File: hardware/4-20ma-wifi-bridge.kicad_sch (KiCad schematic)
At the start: 16 parts, among them J1 Conn_01x19_Female, J2 Conn_01x19_Female, J3 Screw_Terminal_01x02, J4 Screw_Terminal_01x02, M1 DC-DC_Buck_Step_Module-dc-dc_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, SW1 SW_DIP_x01, U1 ESP32-DEVKITC-32D, U2 INA196

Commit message: Added kicad design files
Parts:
- removed U1: ESP32-DEVKITC-32D, MODULE_ESP32-DEVKITC-32D, symbol ESP32-DEVKITC-32D:ESP32-DEVKITC-32D
- removed U2: INA196, Package_TO_SOT_SMD:SOT-23-5, symbol Amplifier_Current:INA196
- added D2: LED, LED_THT:LED_D3.0mm_FlatTop, symbol Device:LED
- added D3, D4: 1N4004, Diode_SMD:D_SMA, symbol Diode:1N4004
- added D5: LED, LED_THT:LED_D1.8mm_W1.8mm_H2.4mm_Horizontal_O1.27mm_Z1.6mm, symbol Device:LED
- added J3, J4: Screw_Terminal_01x02, project_library:TerminalBlock__1x02_P5.00mm_90Degree, symbol Connector:Screw_Terminal_01x02
- added K1, K2: G5V-1, Relay_THT:Relay_SPDT_Omron_G5V-1, symbol Relay:G5V-1
- added Q1, Q2: 2N7002E, Package_TO_SOT_SMD:SOT-23, symbol Transistor_FET:2N7002E
- added R1, R2, R3, R5: 1k, Resistor_SMD:R_0805_2012Metric_Pad1.20x1.40mm_HandSolder, symbol Device:R
- added R4, R6: 10k, Resistor_SMD:R_0805_2012Metric_Pad1.20x1.40mm_HandSolder, symbol Device:R
- added TP1, TP2, TP3: TestPoint, TestPoint:TestPoint_Pad_D1.0mm, symbol Connector:TestPoint
- added U1: ESP32-DEVKITC-32U, MODULE_ESP32-DEVKITC-32U, symbol ESP32-DEVKITC-32U:ESP32-DEVKITC-32U
- added U2: LMP8640, Package_TO_SOT_SMD:SOT-23-6, symbol Amplifier_Current:LMP8640
- D1: footprint LED_THT:LED_D1.8mm_W1.8mm_H2.4mm_Horizontal_O1.27mm_Z4.9mm -> LED_THT:LED_D3.0mm_FlatTop
- R10: renamed from R4; value 4.99 -> 2.7ohm; footprint Resistor_SMD:R_0805_2012Metric_Pad1.20x1.40mm_HandSolder -> Resistor_SMD:R_2512_6332Metric_Pad1.40x3.35mm_HandSolder
- R7: renamed from R1; value 250 -> 1k
- R8: renamed from R2; value 250 -> 1k
- R9: renamed from R3; value 4.99 -> 10k
- renumbered D2 to D6, J3 to J5, J4 to J6
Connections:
- net +3V3: now also TP2.1
- net +5V: now also D3.1 (K), D4.1 (K), K1.2, K2.2, R3.2, R5.2, TP1.1, U2.6 (V+)
- net GND: now also Q1.2 (S), Q2.2 (S), R4.2, R6.2, U2.2 (V-)
- net led1: now also J2.17 (Pin_17), D5.1 (K); no longer D1.1 (K), J2.9 (Pin_9)
- net led2: now also J2.18 (Pin_18); no longer J2.10 (Pin_10)
- net switch: now also J2.19 (Pin_19); no longer J2.2 (Pin_2)
- net vsens: now also J1.3 (Pin_3), TP3.1, U2.1; no longer J1.5 (Pin_5)
- net at R7.1: now also D5.2 (A); no longer D1.2 (A)
- net relay1: now reaches J1.10 (Pin_10)
- net relay1: now also R2.2
- net relay2: now reaches J1.11 (Pin_11)
- net relay2: now also R1.2
- net at J6.1 (Pin_1), R10.1: now also U2.3 (+)
- net at J6.2 (Pin_2), R10.2: now also U2.4 (-)
- new net: J4.1 (Pin_1), K2.5, K2.6
- new net: J4.2 (Pin_2), K2.10
- new net: D2.1 (K), D4.2 (A), K2.9, Q2.3 (D)
- new net: D1.1 (K), D3.2 (A), K1.9, Q1.3 (D)
- new net: Q1.1 (G), R2.1, R4.1
- new net: Q2.1 (G), R1.1, R6.1
- new net: J3.2 (Pin_2), K1.10
- new net: J3.1 (Pin_1), K1.5, K1.6
- new net: D1.2 (A), R3.1
- new net: D2.2 (A), R5.1
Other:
- moved on the sheet: J1, J2

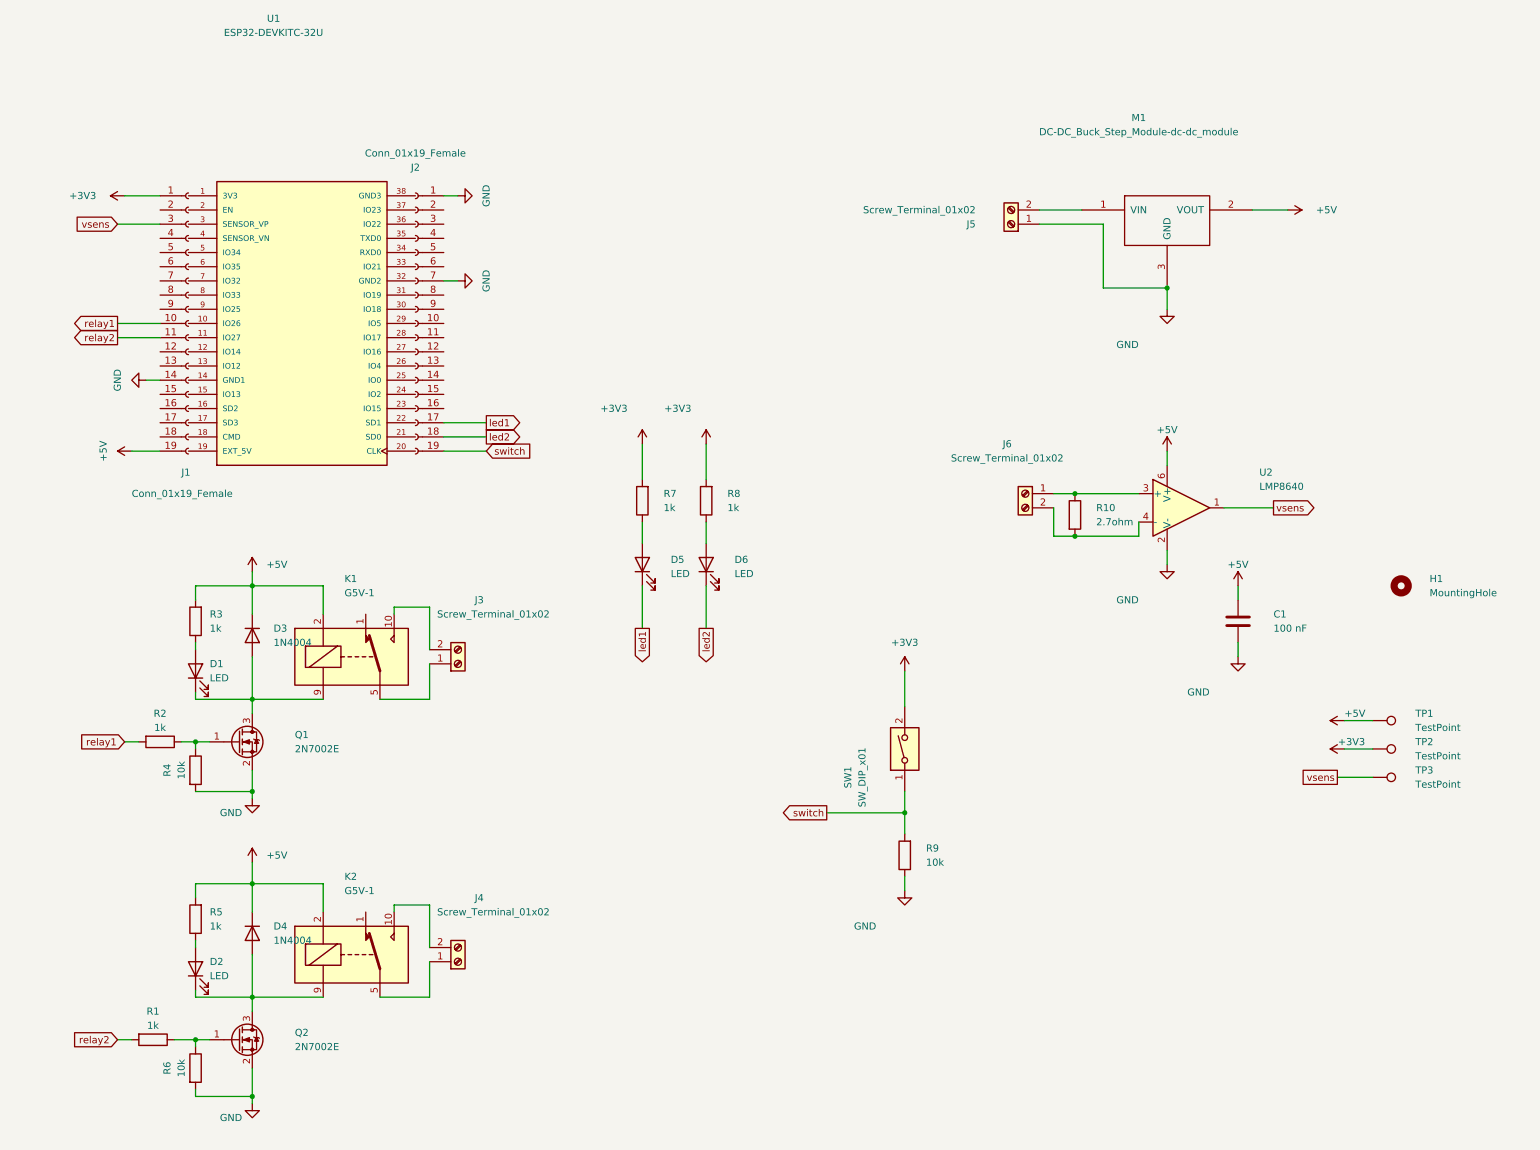
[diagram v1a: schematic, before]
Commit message: Updated schematic and board to fix some erros
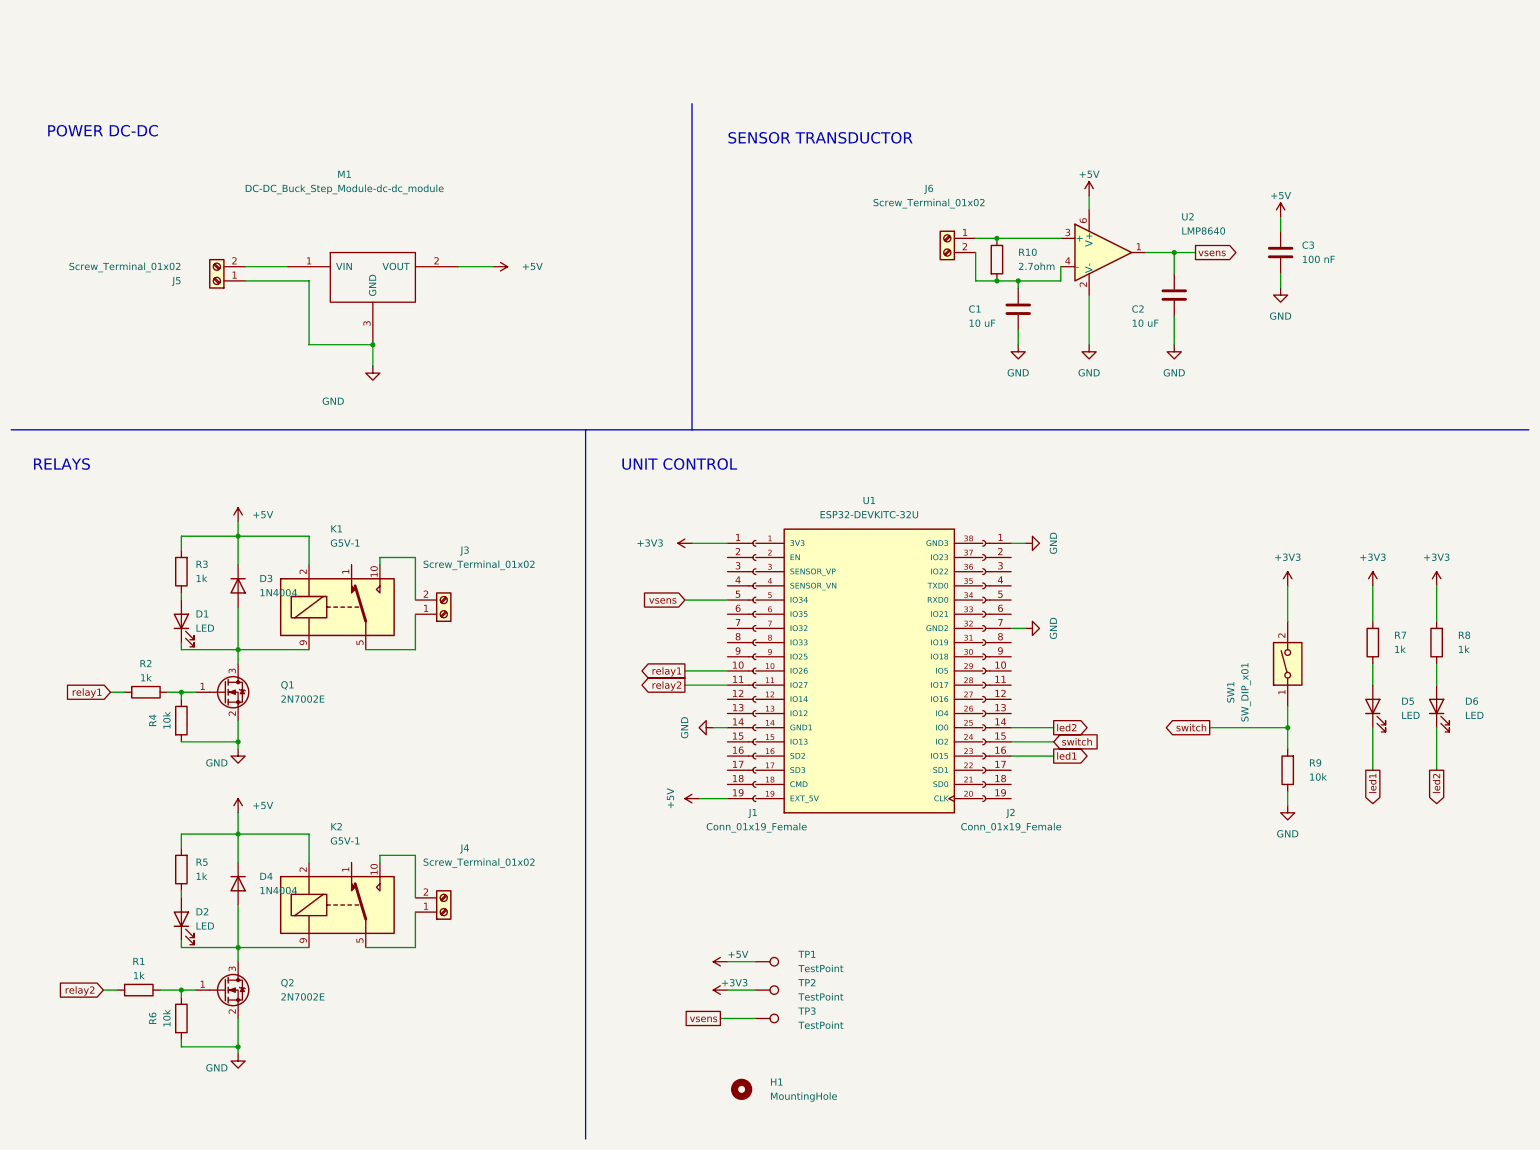
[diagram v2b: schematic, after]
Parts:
- added C1, C2: 10 uF, Capacitor_SMD:C_0805_2012Metric_Pad1.18x1.45mm_HandSolder, symbol Device:C
- renumbered C1 to C3
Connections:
- net GND: now also C1.2, C2.2
- net led1: now also J2.16 (Pin_16); no longer J2.17 (Pin_17)
- net led2: now also J2.14 (Pin_14); no longer J2.18 (Pin_18)
- net switch: now also J2.15 (Pin_15); no longer J2.19 (Pin_19)
- net vsens: now also J1.5 (Pin_5), C2.1; no longer J1.3 (Pin_3)
- net at J6.2 (Pin_2), R10.2, U2.4 (-): now also C1.1
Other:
- note added: "POWER DC-DC"
- note added: "RELAYS"
- note added: "SENSOR TRANSDUCTOR"
- note added: "UNIT CONTROL"
- title: (none) -> 4-20mA Wifi Logger 
- moved on the sheet: C3, D1, D2, D3, D4, D5, D6, H1, J1, J2, J3, J4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
